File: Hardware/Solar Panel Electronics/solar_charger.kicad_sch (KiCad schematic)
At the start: 29 parts, among them J1 Screw_Terminal_SolarPanel_Inp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, J13 Battery Connector, U3 LT3652EDD, U4 LTC4411ES5TRMPBF

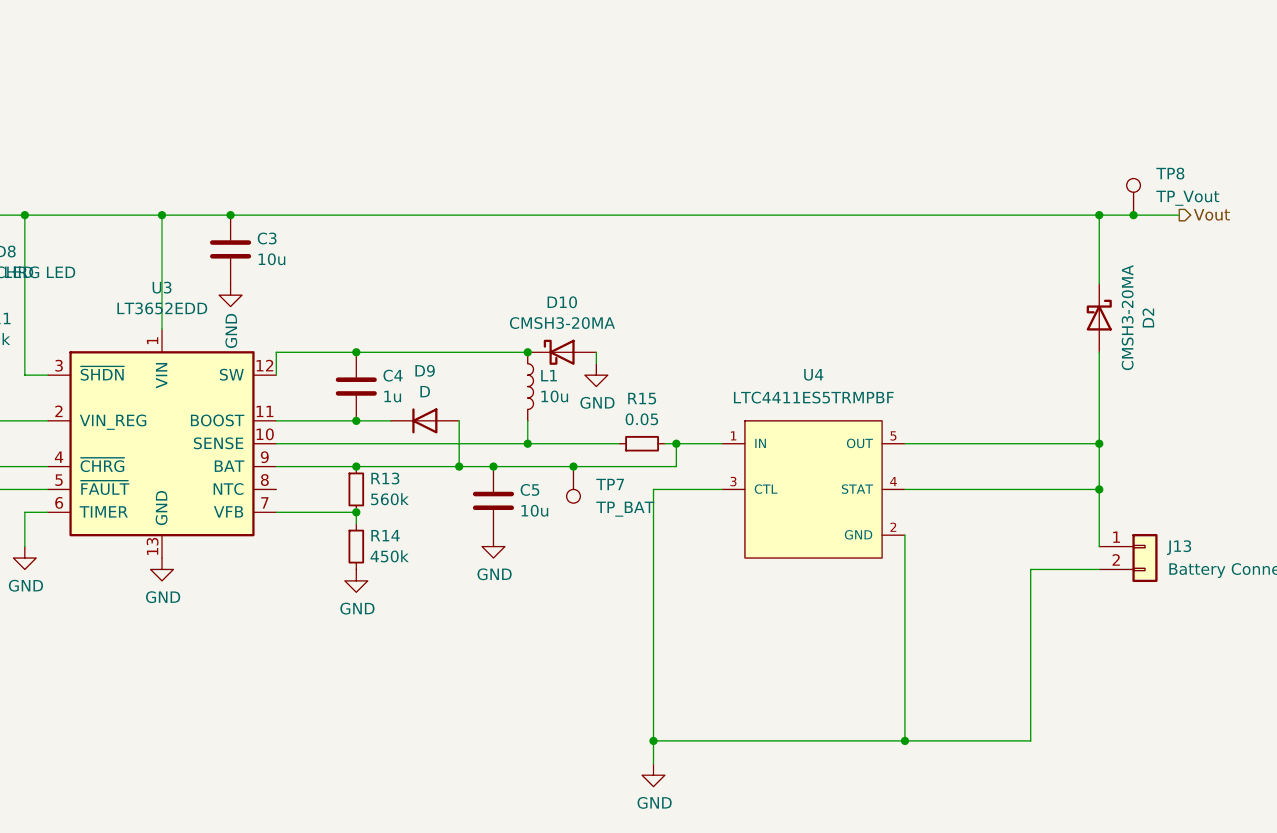
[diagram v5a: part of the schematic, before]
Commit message: removed ltc4411 on solar charger, added solder jumpers
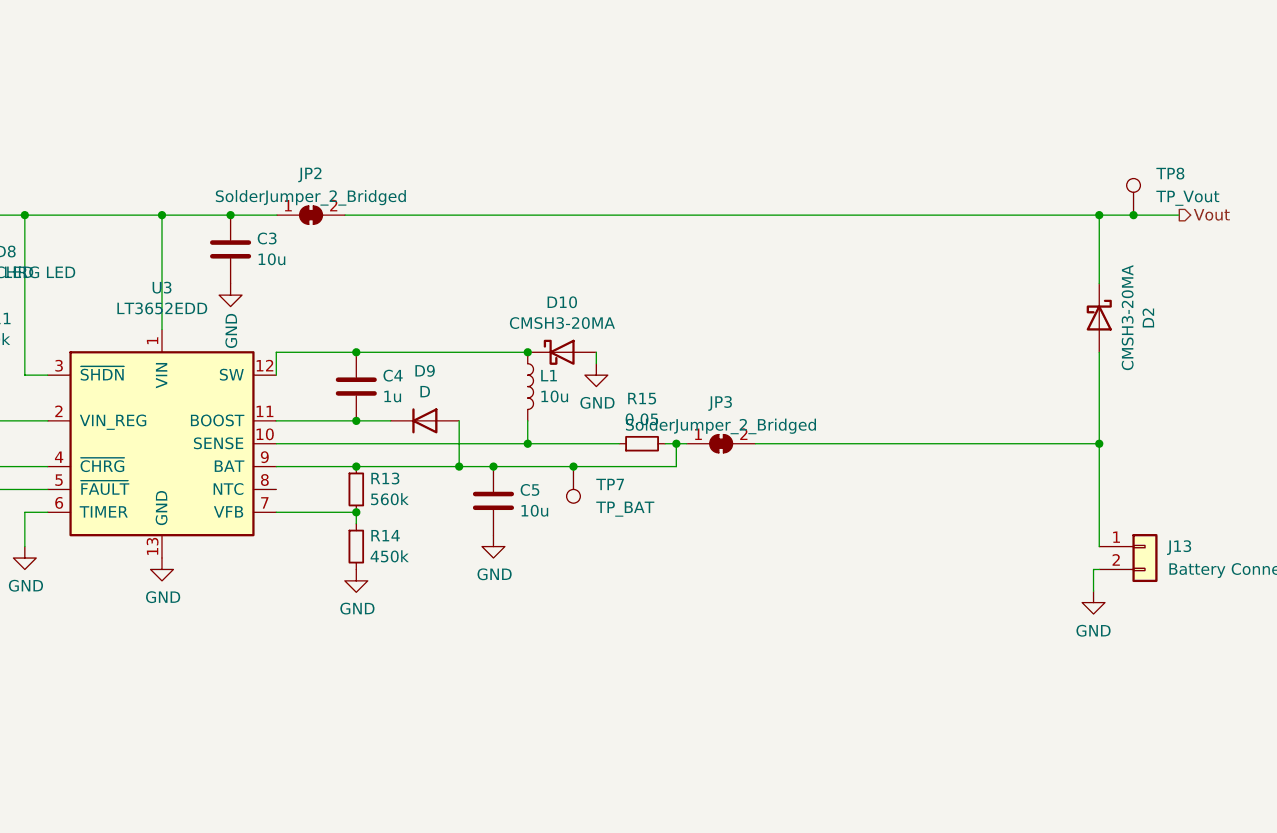
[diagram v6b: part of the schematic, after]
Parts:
- removed U4: LTC4411ES5TRMPBF, LTC4411:Linear_Technology-LTC4411ES5TRMPBF-Level_A, symbol eec:LTC4411ES5TRMPBF
- added JP2, JP3: SolderJumper_2_Bridged, Jumper:SolderJumper-2_P1.3mm_Bridged_RoundedPad1.0x1.5mm, symbol Jumper:SolderJumper_2_Bridged
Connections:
- net Vout: now also JP2.2 (B); no longer C3.2, D6.1 (K), D7.2 (A), D8.2 (A), R8.1, TP6.1, U3.1 (VIN), U3.3 (~{SHDN})
- net at C5.2, D9.2 (A), R13.1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: now also JP3.1 (A)
- net at D2.2 (A), J13.1 (Pin_1): now also JP3.2 (B)
- new net: C3.2, D6.1 (K), D7.2 (A), D8.2 (A), JP2.1 (A), R8.1, TP6.1, U3.1 (VIN), U3.3 (~{SHDN})

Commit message: final?
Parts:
- L1: footprint Inductor_SMD:L_0603_1608Metric -> Inductor_SMD:L_0805_2012Metric
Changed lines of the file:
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@@
       (effects (font (size 1.27 1.27)) (justify left))
     )
-    (property "Footprint" "Inductor_SMD:L_0603_1608Metric" (id 2) (at 128.27 144.78 0)
+    (property "Footprint" "Inductor_SMD:L_0805_2012Metric" (id 2) (at 128.27 144.78 0)
       (effects (font (size 1.27 1.27)) hide)
     )

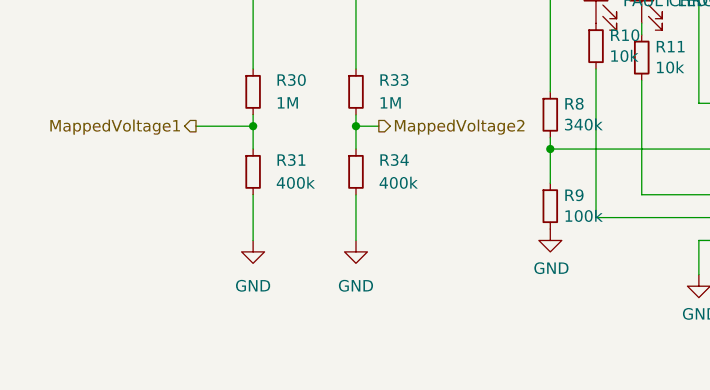
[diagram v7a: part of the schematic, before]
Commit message: attempt to fix vreg and charger
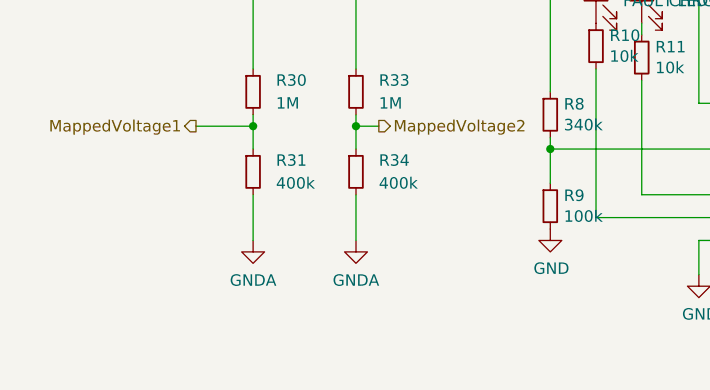
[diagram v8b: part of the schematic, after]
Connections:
- net GND: no longer R31.2, R34.2
- net GNDA: now also R31.2, R34.2
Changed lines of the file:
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@@
     (pin "2")
-  )
-  (symbol (lib_id "power:GND") (at 34.29 158.75 0) (unit 1)
-    (in_bom yes) (on_board yes) (fields_autoplaced)
-    (property "Reference" "#PWR05" (id 0) (at 34.29 165.1 0)
-      (effects (font (size 1.27 1.27)) hide)
-    )
-    (property "Value" "GND" (id 1) (at 34.29 163.83 0))
-    (property "Footprint" "" (id 2) (at 34.29 158.75 0)
-      (effects (font (size 1.27 1.27)) hide)
-    )
-    (property "Datasheet" "" (id 3) (at 34.29 158.75 0)
-      (effects (font (size 1.27 1.27)) hide)
-    )
-    (pin "1")
   )
   (symbol (lib_id "Device:R_Small") (at 34.29 142.24 0) (unit 1)
@@
     (pin "1")
   )
+  (symbol (lib_id "power:GNDA") (at 34.29 158.75 0) (unit 1)
+    (in_bom yes) (on_board yes) (fields_autoplaced)
+    (property "Reference" "#PWR0158" (id 0) (at 34.29 165.1 0)
+      (effects (font (size 1.27 1.27)) hide)
+    )
+    (property "Value" "GNDA" (id 1) (at 34.29 163.1934 0))
+    (property "Footprint" "" (id 2) (at 34.29 158.75 0)
+      (effects (font (size 1.27 1.27)) hide)
+    )
+    (property "Datasheet" "" (id 3) (at 34.29 158.75 0)
+      (effects (font (size 1.27 1.27)) hide)
+    )
+    (pin "1")
+  )
   (symbol (lib_id "Connector:TestPoint") (at 195.58 125.73 0) (unit 1)
     (in_bom yes) (on_board yes) (fields_autoplaced)
@@
     (pin "1")
   )
-  (symbol (lib_id "power:GND") (at 22.86 158.75 0) (unit 1)
-    (in_bom yes) (on_board yes) (fields_autoplaced)
-    (property "Reference" "#PWR04" (id 0) (at 22.86 165.1 0)
-      (effects (font (size 1.27 1.27)) hide)
-    )
-    (property "Value" "GND" (id 1) (at 22.86 163.83 0))
+  (symbol (lib_id "Connector:TestPoint") (at 52.07 125.73 0) (unit 1)
+    (in_bom yes) (on_board yes) (fields_autoplaced)
+    (property "Reference" "TP6" (id 0) (at 54.61 121.1579 0)
+      (effects (font (size 1.27 1.27)) (justify left))
+    )
+    (property "Value" "TP_Vsolarpanel" (id 1) (at 54.61 123.6979 0)
+      (effects (font (size 1.27 1.27)) (justify left))
+    )
+    (property "Footprint" "TestPoint:TestPoint_Pad_D1.0mm" (id 2) (at 57.15 125.73 0)
+      (effects (font (size 1.27 1.27)) hide)
+    )
+    (property "Datasheet" "~" (id 3) (at 57.15 125.73 0)
+      (effects (font (size 1.27 1.27)) hide)
+    )
+    (pin "1")
+  )
+  (symbol (lib_id "Device:R_Small") (at 22.86 151.13 0) (unit 1)
+    (in_bom yes) (on_board yes) (fields_autoplaced)
+    (property "Reference" "R31" (id 0) (at 25.4 149.8599 0)
+      (effects (font (size 1.27 1.27)) (justify left))
+    )
+    (property "Value" "400k" (id 1) (at 25.4 152.3999 0)
+      (effects (font (size 1.27 1.27)) (justify left))
+    )
+    (property "Footprint" "Resistor_SMD:R_0603_1608Metric" (id 2) (at 22.86 151.13 0)
+      (effects (font (size 1.27 1.27)) hide)
+    )
+    (property "Datasheet" "~" (id 3) (at 22.86 151.13 0)
+      (effects (font (size 1.27 1.27)) hide)
+    )
+    (pin "1")
+    (pin "2")
+  )
+  (symbol (lib_id "power:GNDA") (at 22.86 158.75 0) (unit 1)
+    (in_bom yes) (on_board yes) (fields_autoplaced)
+    (property "Reference" "#PWR0159" (id 0) (at 22.86 165.1 0)
+      (effects (font (size 1.27 1.27)) hide)
+    )
+    (property "Value" "GNDA" (id 1) (at 22.86 163.1934 0))
     (property "Footprint" "" (id 2) (at 22.86 158.75 0)
       (effects (font (size 1.27 1.27)) hide)
@@
     (pin "1")
   )
-  (symbol (lib_id "Connector:TestPoint") (at 52.07 125.73 0) (unit 1)
-    (in_bom yes) (on_board yes) (fields_autoplaced)
-    (property "Reference" "TP6" (id 0) (at 54.61 121.1579 0)
-      (effects (font (size 1.27 1.27)) (justify left))
-    )
-    (property "Value" "TP_Vsolarpanel" (id 1) (at 54.61 123.6979 0)
-      (effects (font (size 1.27 1.27)) (justify left))
-    )
-    (property "Footprint" "TestPoint:TestPoint_Pad_D1.0mm" (id 2) (at 57.15 125.73 0)
-      (effects (font (size 1.27 1.27)) hide)
-    )
-    (property "Datasheet" "~" (id 3) (at 57.15 125.73 0)
-      (effects (font (size 1.27 1.27)) hide)
-    )
-    (pin "1")
-  )
-  (symbol (lib_id "Device:R_Small") (at 22.86 151.13 0) (unit 1)
-    (in_bom yes) (on_board yes) (fields_autoplaced)
-    (property "Reference" "R31" (id 0) (at 25.4 149.8599 0)
-      (effects (font (size 1.27 1.27)) (justify left))
-    )
-    (property "Value" "400k" (id 1) (at 25.4 152.3999 0)
-      (effects (font (size 1.27 1.27)) (justify left))
-    )
-    (property "Footprint" "Resistor_SMD:R_0603_1608Metric" (id 2) (at 22.86 151.13 0)
-      (effects (font (size 1.27 1.27)) hide)
-    )
-    (property "Datasheet" "~" (id 3) (at 22.86 151.13 0)
-      (effects (font (size 1.27 1.27)) hide)
-    )
-    (pin "1")
-    (pin "2")
-  )
   (symbol (lib_id "Jumper:SolderJumper_2_Bridged") (at 104.1908 125.73 0) (unit 1)
